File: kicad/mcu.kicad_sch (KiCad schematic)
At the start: 3 parts, among them J8 Conn_01x04, U4 ESP32-C6-DEVKITC-1-N8

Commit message: Reviewed the ESP32-C6-DEVKIT GPIO's. Some of them have a dual function and are better left untouched.
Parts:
- J8: value Conn_01x04 -> Conn_01x05; footprint Connector_PinHeader_2.54mm:PinHeader_1x04_P2.54mm_Vertical -> Connector_PinHeader_2.54mm:PinHeader_1x05_P2.54mm_Vertical; symbol Connector_Generic:Conn_01x04 -> Connector_Generic:Conn_01x05
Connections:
- net ENABLE is gone; now on net DIR: U4.J1_6 (GPIO7)
- net +3V3: now also J8.4 (Pin_4)
- net DIR: no longer U4.J1_7 (GPIO0)
- net GND: now also J8.5 (Pin_5); no longer J8.4 (Pin_4)
- net SCLK: now also U4.J1_8 (GPIO1); no longer U4.J1_9 (GPIO8)
- net STEP: now also U4.J1_7 (GPIO0); no longer U4.J1_8 (GPIO1)
- net at J8.1 (Pin_1): now also U4.J3_8 (GPIO20); no longer U4.J3_11 (GPIO9)
- net at J8.2 (Pin_2): now also U4.J3_9 (GPIO19); no longer U4.J3_13 (GPIO13)
- net at J8.3 (Pin_3): now also U4.J3_10 (GPIO18); no longer U4.J3_14 (GPIO12)
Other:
- note added: "RGB-LED"
- note added: "USB"

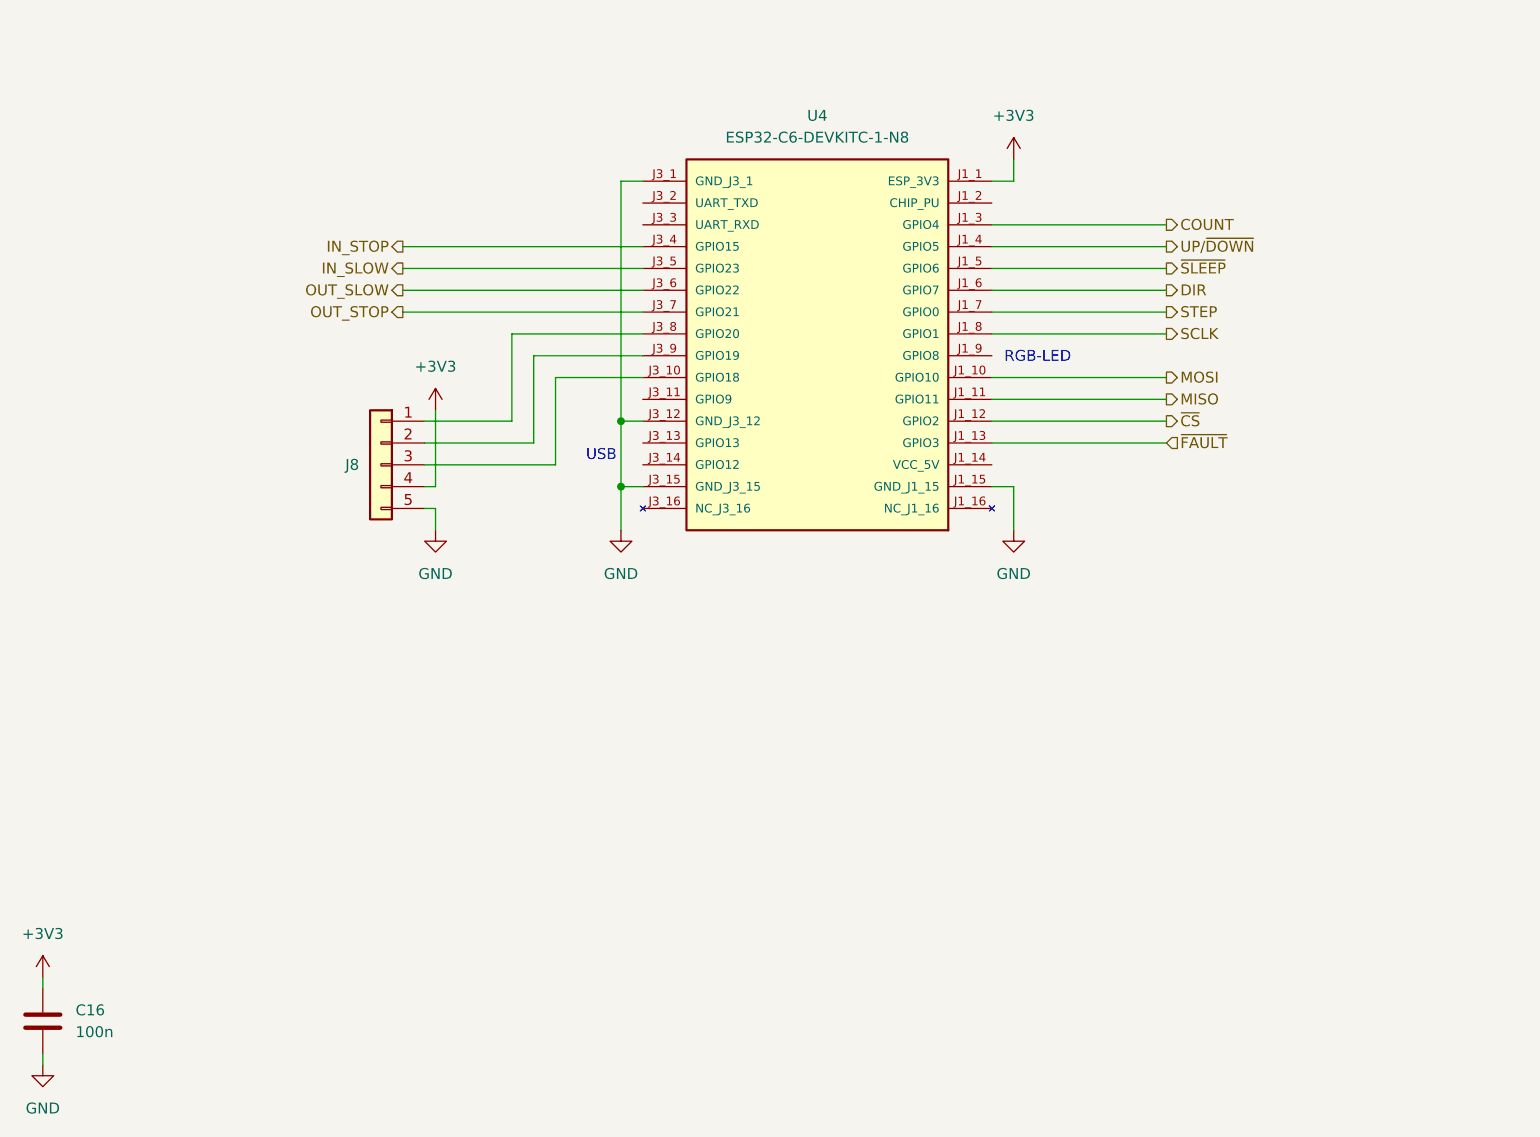
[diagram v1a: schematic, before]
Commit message: Supplying the ESP32-C6-DEVKIT with 5V and using its 3V3 output to supply the boards logic. Removed the 3V3 switch mode power supply on the board.
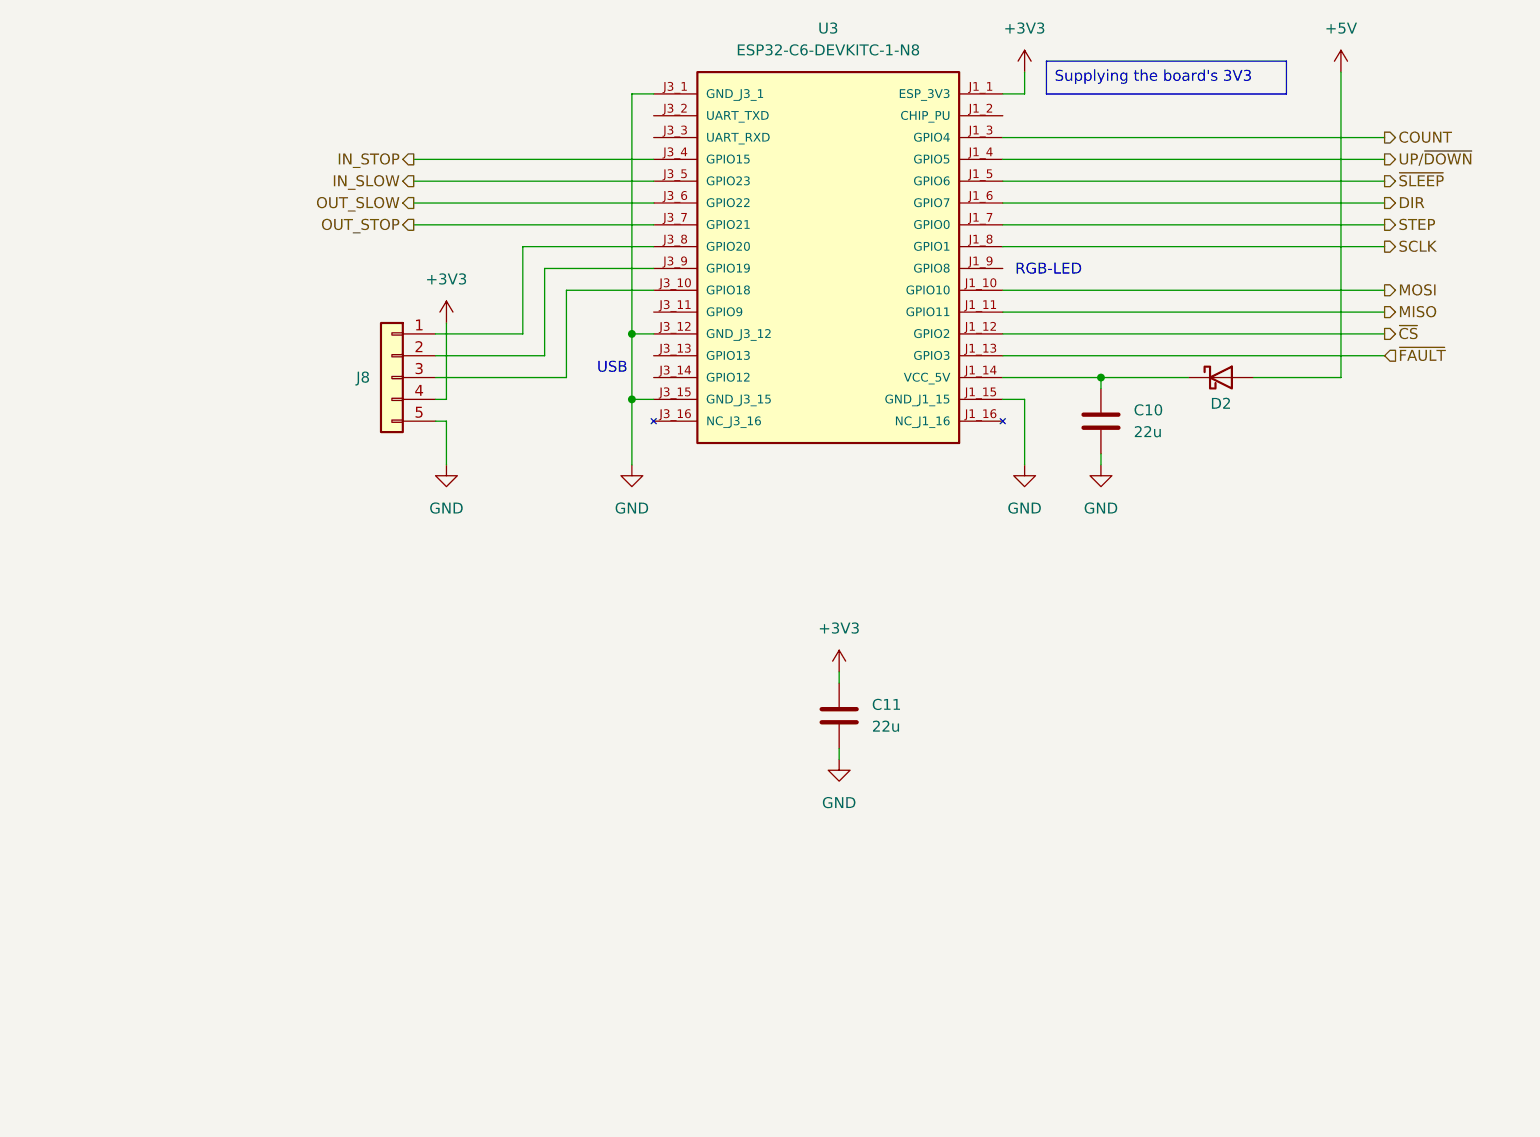
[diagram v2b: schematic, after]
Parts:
- removed C16: 100n, Capacitor_SMD:C_0603_1608Metric, symbol Device:C
- added C10, C11: 22u, Capacitor_SMD:C_1206_3216Metric, symbol Device:C
- added D2: 1N5819HW-7-F, Diode_SMD:D_SOD-123, symbol Diode:1N5819
- renumbered U4 to U3
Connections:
- net +3V3: now also C11.1
- net GND: now also C10.2, C11.2
- net at U3.J1_14 (VCC_5V): now also C10.1, D2.1 (K)
- new net +5V: D2.2 (A)
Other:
- moved on the sheet: J8, U3

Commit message: Version 1.0 files as send to PCBWay
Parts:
- J8, U3: now not fitted
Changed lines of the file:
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@@
 		(in_bom yes)
 		(on_board yes)
-		(dnp no)
+		(dnp yes)
 		(property "Reference" "J8"
 			(at 91.44 99.0599 0)
@@
 		(in_bom yes)
 		(on_board yes)
-		(dnp no)
+		(dnp yes)
 		(fields_autoplaced yes)
 		(property "Reference" "U3"

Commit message: Updated to use more of JCLPCB's basic components. Added extra field "FT Rotation Offset" to get the correct orientation for placement at JCLPCB.
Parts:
- C10, C11: Dielectric X7S -> (none); LCSC (none) -> C12891; MF Murata -> Samsung; MP GRM31CC71C226ME11L -> CL31A226KAHNNNE; SupplierPN 490-17691-1-ND -> 1276-3047-1-ND; Voltage 16V -> 25V
- D2: value 1N5819HW-7-F -> 1N5819WS; footprint Diode_SMD:D_SOD-123 -> Diode_SMD:D_SOD-323; LCSC (none) -> C191023; MF Diodes Incorporated -> Guangdong Hottech; MP 1N5819HW-7-F -> 1N5819WS; SupplierPN 1N5819HW-FDICT-ND -> 5399-1N5819WSCT-ND
- J8: LCSC (none) -> C6461551; MP 61300411121 -> 61300511121
- U3: LCSC (none) -> C20554022
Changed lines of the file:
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@@
 	(title_block
 		(title "TV slider")
-		(date "2025-12-23")
-		(rev "1.0")
+		(date "2026-01-03")
+		(rev "${REVISION}")
 		(company "NX Solutions")
 	)
@@
 			)
 		)
-		(property "Dielectric" "X7S"
+		(property "Dielectric" ""
 			(at 176.53 104.14 0)
 			(effects
@@
 			)
 		)
-		(property "SupplierPN" "490-17691-1-ND"
+		(property "SupplierPN" "1276-3047-1-ND"
 			(at 176.53 104.14 0)
 			(effects
@@
 			)
 		)
-		(property "MF" "Murata"
+		(property "MF" "Samsung"
 			(at 176.53 104.14 0)
 			(effects
@@
 			)
 		)
-		(property "MP" "GRM31CC71C226ME11L"
+		(property "MP" "CL31A226KAHNNNE"
 			(at 176.53 104.14 0)
 			(effects
@@
 			)
 		)
-		(property "Voltage" "16V"
+		(property "Voltage" "25V"
 			(at 176.53 104.14 0)
 			(effects
@@
 		)
 		(property "SNAPEDA_PN" ""
+			(at 176.53 104.14 0)
+			(effects
+				(font
+					(size 1.27 1.27)
+				)
+				(hide yes)
+			)
+		)
+		(property "LCSC" "C12891"
+			(at 176.53 104.14 0)
+			(effects
+				(font
+					(size 1.27 1.27)
+				)
+				(hide yes)
+			)
+		)
+		(property "FT Rotation Offset" ""
 			(at 176.53 104.14 0)
 			(effects
@@
 			)
 		)
-		(property "Dielectric" "X7S"
+		(property "Dielectric" ""
 			(at 146.05 138.43 0)
 			(effects
@@
 			)
 		)
-		(property "SupplierPN" "490-17691-1-ND"
+		(property "SupplierPN" "1276-3047-1-ND"
 			(at 146.05 138.43 0)
 			(effects
@@
 			)
 		)
-		(property "MF" "Murata"
+		(property "MF" "Samsung"
 			(at 146.05 138.43 0)
 			(effects
@@
 			)
 		)
-		(property "MP" "GRM31CC71C226ME11L"
+		(property "MP" "CL31A226KAHNNNE"
 			(at 146.05 138.43 0)
 			(effects
@@
 			)
 		)
-		(property "Voltage" "16V"
+		(property "Voltage" "25V"
 			(at 146.05 138.43 0)
 			(effects
@@
 		)
 		(property "SNAPEDA_PN" ""
+			(at 146.05 138.43 0)
+			(effects
+				(font
+					(size 1.27 1.27)
+				)
+				(hide yes)
+			)
+		)
+		(property "LCSC" "C12891"
+			(at 146.05 138.43 0)
+			(effects
+				(font
+					(size 1.27 1.27)
+				)
+				(hide yes)
+			)
+		)
+		(property "FT Rotation Offset" ""
 			(at 146.05 138.43 0)
 			(effects
@@
 			)
 		)
-		(property "MP" "61300411121"
+		(property "MP" "61300511121"
 			(at 93.98 99.06 0)
 			(effects
@@
 		)
 		(property "SupplierPN" "732-5317-ND"
+			(at 93.98 99.06 0)
+			(effects
+				(font
+					(size 1.27 1.27)
+				)
+				(hide yes)
+			)
+		)
+		(property "LCSC" "C6461551"
+			(at 93.98 99.06 0)
+			(effects
+				(font
+					(size 1.27 1.27)
+				)
+				(hide yes)
+			)
+		)
+		(property "FT Rotation Offset" ""
 			(at 93.98 99.06 0)
 			(effects
@@
 			)
 		)
+		(property "LCSC" "C20554022"
+			(at 144.78 86.36 0)
+			(effects
+				(font
+					(size 1.27 1.27)
+				)
+				(hide yes)
+			)
+		)
+		(property "FT Rotation Offset" ""
+			(at 144.78 86.36 0)
+			(effects
+				(font
+					(size 1.27 1.27)
+				)
+				(hide yes)
+			)
+		)
 		(pin "J1_13"
 		)
@@
 			)
 		)
-		(property "Value" "1N5819HW-7-F"
+		(property "Value" "1N5819WS"
 			(at 191.008 104.14 0)
 			(effects
@@
 			)
 		)
-		(property "Footprint" "Diode_SMD:D_SOD-123"
+		(property "Footprint" "Diode_SMD:D_SOD-323"
 			(at 190.5 103.505 0)
 			(effects
@@
 			)
 		)
-		(property "MF" "Diodes Incorporated"
+		(property "MF" "Guangdong Hottech"
 			(at 190.5 99.06 0)
 			(effects
@@
 			)
 		)
-		(property "MP" "1N5819HW-7-F"
+		(property "MP" " 1N5819WS"
 			(at 190.5 99.06 0)
 			(effects
@@
 			)
 		)
-		(property "SupplierPN" "1N5819HW-FDICT-ND"
+		(property "SupplierPN" "5399-1N5819WSCT-ND"
 			(at 190.5 99.06 0)
 			(effects
@@
 			(at 190.5 99.06 0)
 			(effects
+				(font
+					(size 1.27 1.27)
+				)
+				(hide yes)
+			)
+		)
+		(property "LCSC" "C191023"
+			(at 190.5 99.06 0)
+			(effects
+				(font
+					(size 1.27 1.27)
+				)
+				(hide yes)
+			)
+		)
+		(property "FT Rotation Offset" ""
+			(at 190.5 99.06 0)
+			(effects

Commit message: Fixed part number for DNP component.
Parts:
- J8: SupplierPN 732-5317-ND -> 732-5318-ND
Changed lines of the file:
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@@
 			)
 		)
-		(property "SupplierPN" "732-5317-ND"
+		(property "SupplierPN" "732-5318-ND"
 			(at 93.98 99.06 0)
 			(effects
